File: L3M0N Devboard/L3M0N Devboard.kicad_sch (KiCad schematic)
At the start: 13 parts, among them U2 RP2040

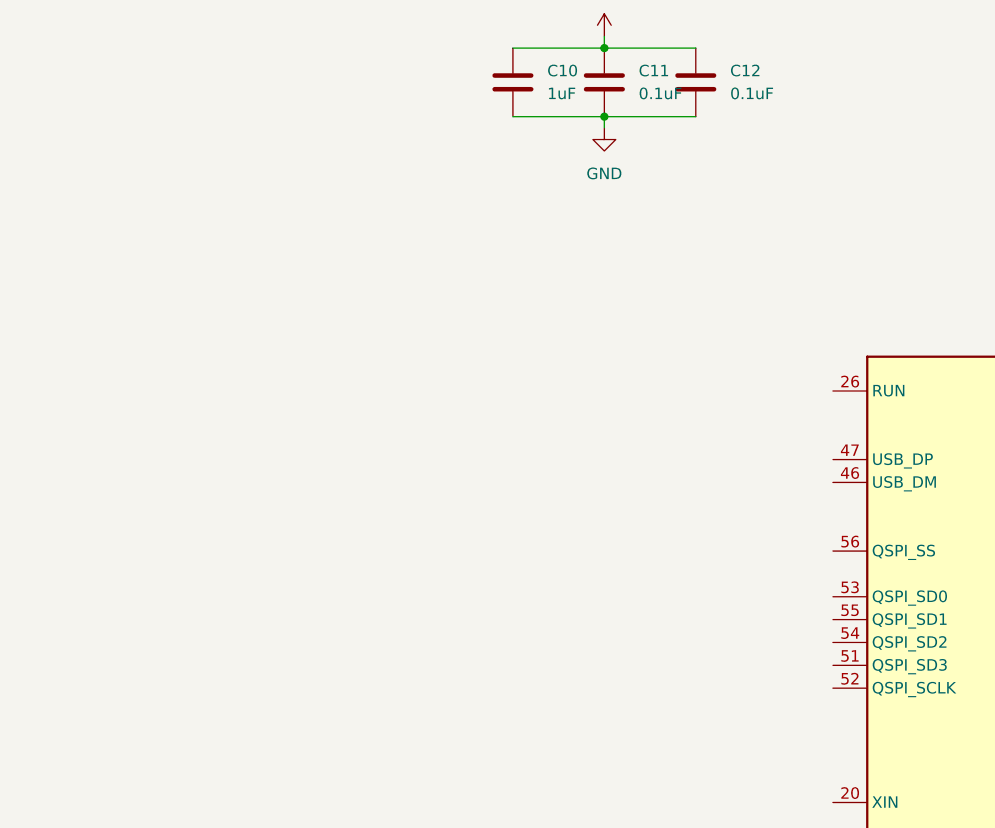
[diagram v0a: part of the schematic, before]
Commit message: Added USB C receptacle
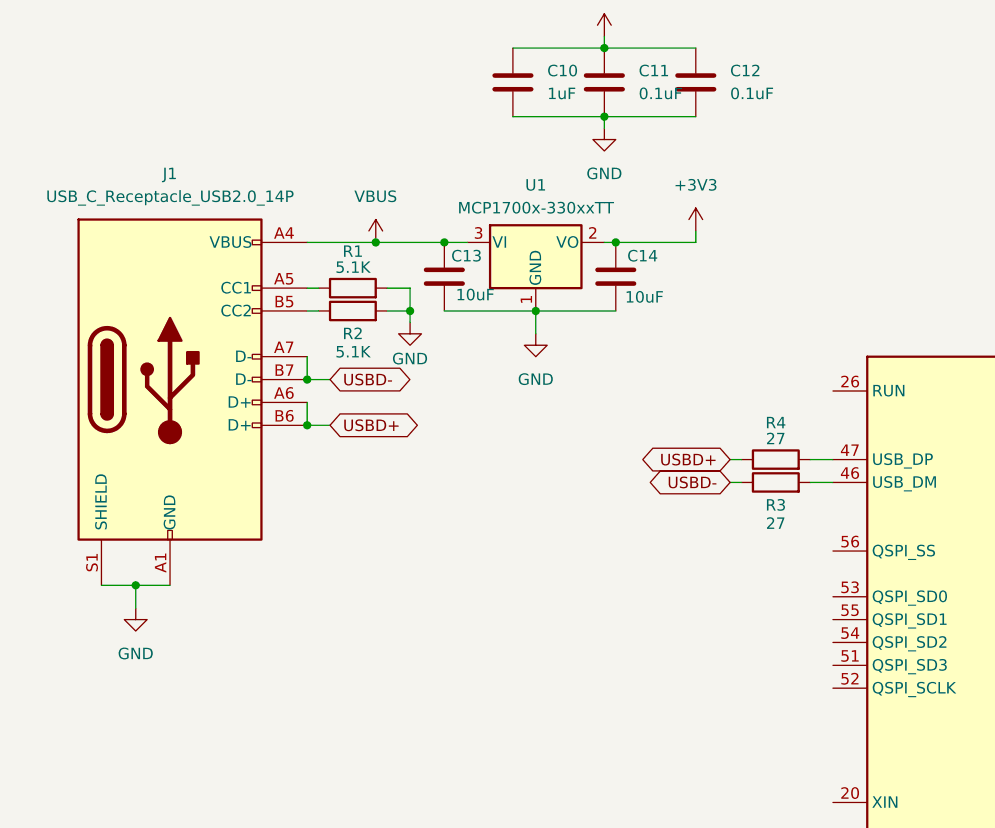
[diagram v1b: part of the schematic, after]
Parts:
- added C13, C14: 10uF, symbol Device:C
- added J1: USB_C_Receptacle_USB2.0_14P, symbol Connector:USB_C_Receptacle_USB2.0_14P
- added R1, R2: 5.1K, symbol Device:R
- added R3, R4: 27, symbol Device:R
- added U1: MCP1700x-330xxTT, Package_TO_SOT_SMD:SOT-23, symbol Regulator_Linear:MCP1700x-330xxTT
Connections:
- net +3V3: now also C14.1, U1.2 (VO)
- net GND: now also C13.2, C14.2, J1.A1 (GND), J1.A12 (GND), J1.B1 (GND), J1.B12 (GND), J1.S1 (SHIELD), R1.2, R2.2, U1.1 (GND)
- net at U2.46 (USB_DM): now also R3.2
- net at U2.47 (USB_DP): now also R4.2
- new net: J1.B5 (CC2), R2.1
- new net: J1.A5 (CC1), R1.1
- new net USBD+: J1.A6 (D+), J1.B6 (D+), R4.1
- new net USBD-: J1.A7 (D-), J1.B7 (D-), R3.1
- new net VBUS: C13.1, J1.A4 (VBUS), J1.A9 (VBUS), J1.B4 (VBUS), J1.B9 (VBUS), U1.3 (VI)

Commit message: Added crystal oscilator
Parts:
- added C15, C16: 33pF, symbol Device:C
- added R5: 1K, symbol Device:R
- added Y1: 12 MHz, symbol Device:Crystal_GND24
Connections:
- net GND: now also C15.2, C16.1, Y1.2, Y1.4
- net XIN: now reaches U2.20 (XIN)
- net XIN: now also C15.1, Y1.3
- net XOUT: now reaches U2.21 (XOUT)
- net XOUT: now also R5.2
- new net: C16.2, R5.1, Y1.1

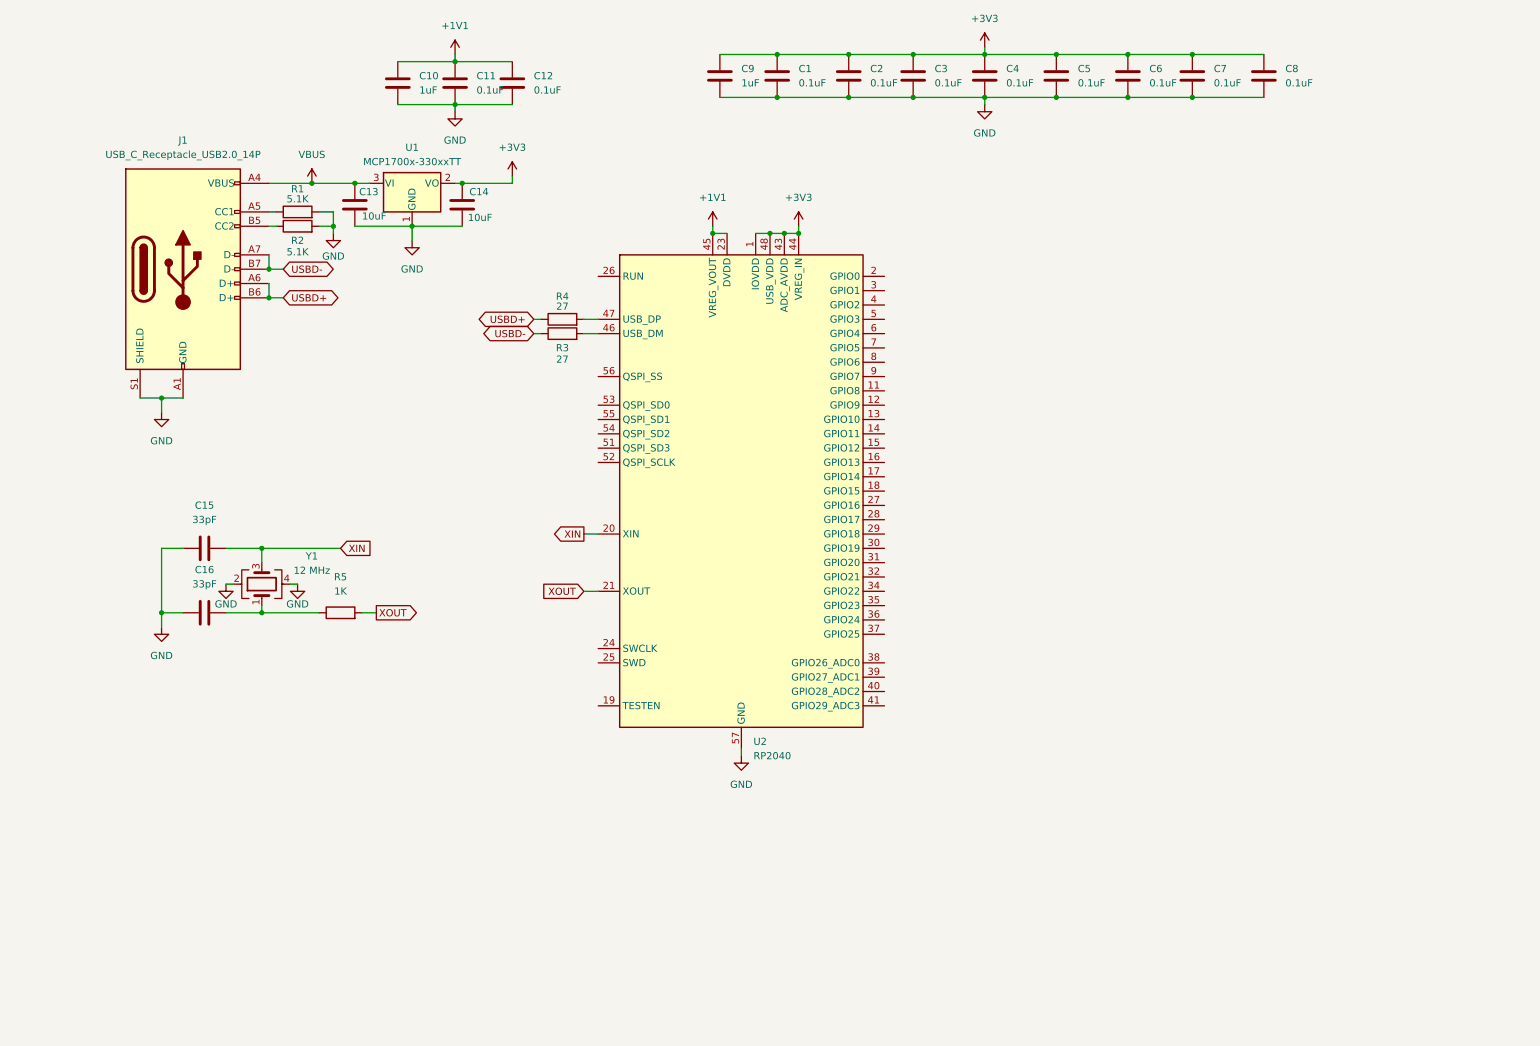
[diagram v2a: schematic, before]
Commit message: Assigned footrprints
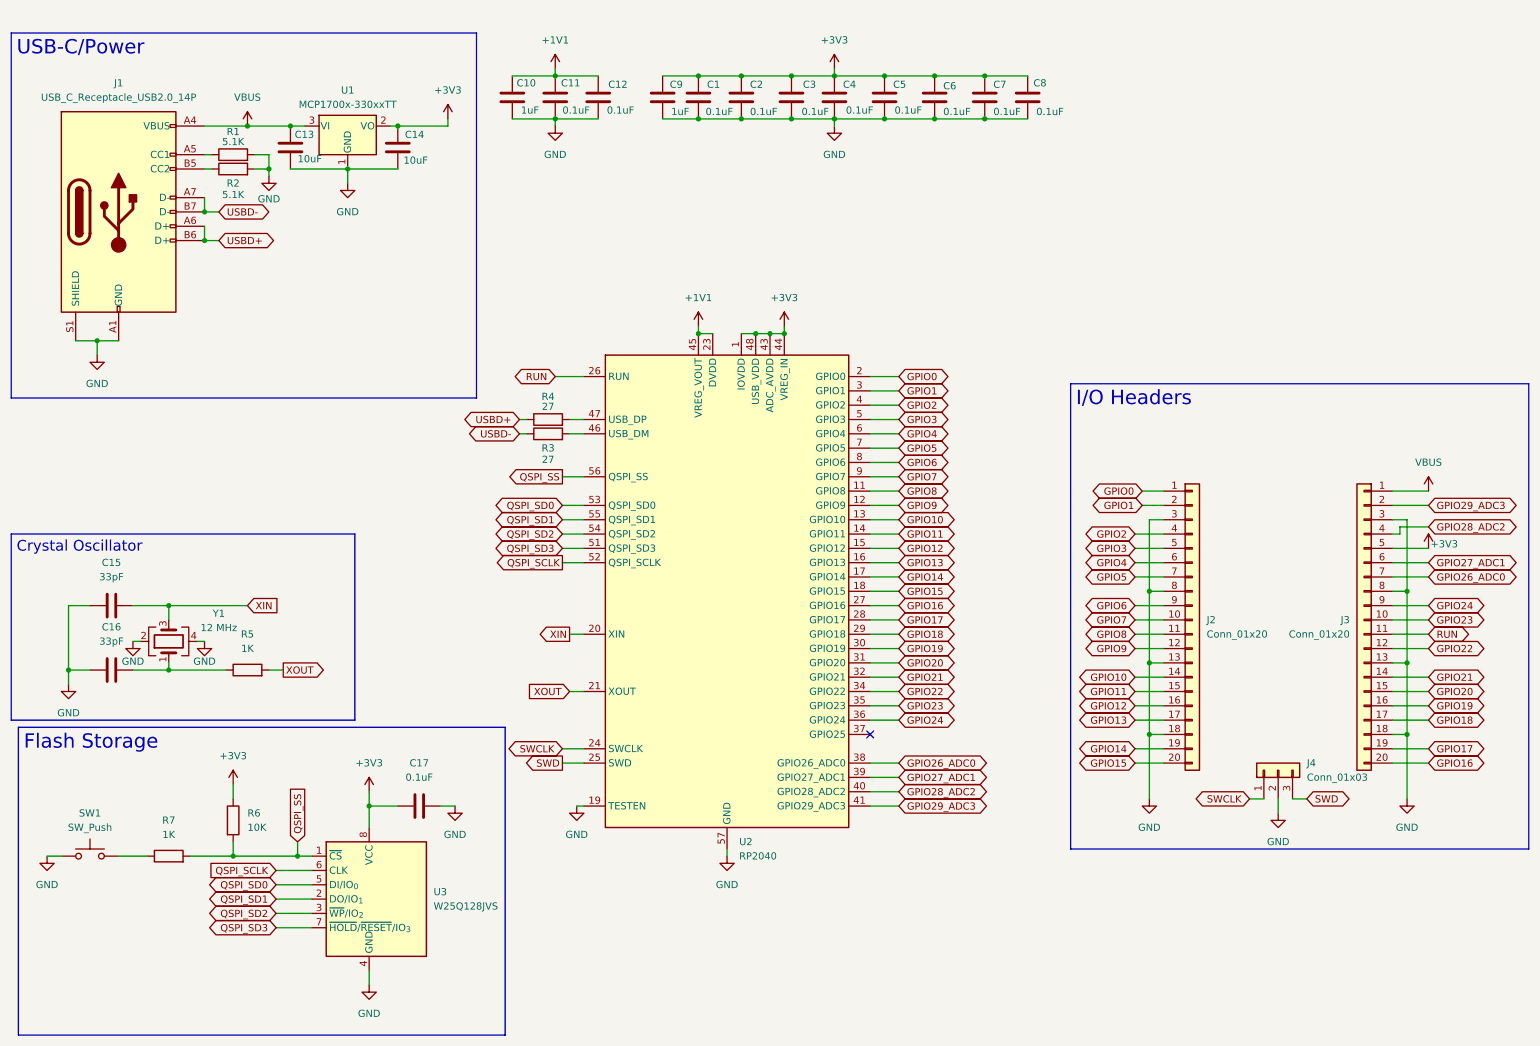
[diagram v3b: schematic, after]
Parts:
- added C17: 0.1uF, Capacitor_SMD:C_0402_1005Metric, symbol Device:C
- added J2, J3: Conn_01x20, Connector_PinHeader_2.54mm:PinHeader_1x20_P2.54mm_Vertical, symbol Connector_Generic:Conn_01x20
- added J4: Conn_01x03, Connector_PinHeader_2.54mm:PinHeader_1x03_P2.54mm_Vertical, symbol Connector_Generic:Conn_01x03
- added R6: 10K, Resistor_SMD:R_0402_1005Metric, symbol Device:R
- added R7: 1K, Resistor_SMD:R_0402_1005Metric, symbol Device:R
- added SW1: SW_Push, Button_Switch_SMD:SW_Push_SPST_NO_Alps_SKRK, symbol Switch:SW_Push
- added U3: W25Q128JVS, Package_SO:SOIC-8_5.3x5.3mm_P1.27mm, symbol Memory_Flash:W25Q128JVS
- C1, C10, C11, C12, C15, C16, C2, C3, C4, C5, C6, C7, C8, C9: footprint (none) -> Capacitor_SMD:C_0402_1005Metric
- C13, C14: footprint (none) -> Capacitor_SMD:C_0603_1608Metric
- J1: footprint (none) -> Connector_USB:USB_C_Receptacle_HRO_TYPE-C-31-M-12
- R1, R2, R3, R4, R5: footprint (none) -> Resistor_SMD:R_0402_1005Metric
- Y1: footprint (none) -> Crystal:Crystal_SMD_3225-4Pin_3.2x2.5mm
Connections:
- net +3V3: now also C17.1, J3.5 (Pin_5), R6.1, U3.8 (VCC)
- net GND: now also U2.19 (TESTEN), C17.2, J2.13 (Pin_13), J2.18 (Pin_18), J2.3 (Pin_3), J2.8 (Pin_8), J3.13 (Pin_13), J3.18 (Pin_18), J3.3 (Pin_3), J3.8 (Pin_8), J4.2 (Pin_2), SW1.1, U3.4 (GND)
- net VBUS: now also J3.1 (Pin_1)
- net GPIO8: now reaches U2.11 (GPIO8)
- net GPIO8: now also J2.11 (Pin_11)
- net GPIO9: now reaches U2.12 (GPIO9)
- net GPIO9: now also J2.12 (Pin_12)
- net GPIO10: now reaches U2.13 (GPIO10)
- net GPIO10: now also J2.14 (Pin_14)
- net GPIO11: now reaches U2.14 (GPIO11)
- net GPIO11: now also J2.15 (Pin_15)
- net GPIO12: now reaches U2.15 (GPIO12)
- net GPIO12: now also J2.16 (Pin_16)
- net GPIO13: now reaches U2.16 (GPIO13)
- net GPIO13: now also J2.17 (Pin_17)
- net GPIO14: now reaches U2.17 (GPIO14)
- net GPIO14: now also J2.19 (Pin_19)
- net GPIO15: now reaches U2.18 (GPIO15)
- net GPIO15: now also J2.20 (Pin_20)
- net GPIO0: now reaches U2.2 (GPIO0)
- net GPIO0: now also J2.1 (Pin_1)
- net SWCLK: now reaches U2.24 (SWCLK)
- net SWCLK: now also J4.1 (Pin_1)
- net SWD: now reaches U2.25 (SWD)
- net SWD: now also J4.3 (Pin_3)
- net RUN: now reaches U2.26 (RUN)
- net RUN: now also J3.11 (Pin_11)
- net GPIO16: now reaches U2.27 (GPIO16)
- net GPIO16: now also J3.20 (Pin_20)
- net GPIO17: now reaches U2.28 (GPIO17)
- net GPIO17: now also J3.19 (Pin_19)
- net GPIO18: now reaches U2.29 (GPIO18)
- net GPIO18: now also J3.17 (Pin_17)
- net GPIO1: now reaches U2.3 (GPIO1)
- net GPIO1: now also J2.2 (Pin_2)
- net GPIO19: now reaches U2.30 (GPIO19)
- net GPIO19: now also J3.16 (Pin_16)
- net GPIO20: now reaches U2.31 (GPIO20)
- net GPIO20: now also J3.15 (Pin_15)
- net GPIO21: now reaches U2.32 (GPIO21)
- net GPIO21: now also J3.14 (Pin_14)
- net GPIO22: now reaches U2.34 (GPIO22)
- net GPIO22: now also J3.12 (Pin_12)
- net GPIO23: now reaches U2.35 (GPIO23)
- net GPIO23: now also J3.10 (Pin_10)
- net GPIO24: now reaches U2.36 (GPIO24)
- net GPIO24: now also J3.9 (Pin_9)
- net GPIO26_ADC0: now reaches U2.38 (GPIO26_ADC0)
- net GPIO26_ADC0: now also J3.7 (Pin_7)
- net GPIO27_ADC1: now reaches U2.39 (GPIO27_ADC1)
- net GPIO27_ADC1: now also J3.6 (Pin_6)
- net GPIO2: now reaches U2.4 (GPIO2)
- net GPIO2: now also J2.4 (Pin_4)
- net GPIO28_ADC2: now reaches U2.40 (GPIO28_ADC2)
- net GPIO28_ADC2: now also J3.4 (Pin_4)
- net GPIO29_ADC3: now reaches U2.41 (GPIO29_ADC3)
- net GPIO29_ADC3: now also J3.2 (Pin_2)
- net GPIO3: now reaches U2.5 (GPIO3)
- net GPIO3: now also J2.5 (Pin_5)
- net QSPI_SD3: now reaches U2.51 (QSPI_SD3)
- net QSPI_SD3: now also U3.7 (~{HOLD}/~{RESET}/IO_{3})
- net QSPI_SCLK: now reaches U2.52 (QSPI_SCLK)
- net QSPI_SCLK: now also U3.6 (CLK)
- net QSPI_SD0: now reaches U2.53 (QSPI_SD0)
- net QSPI_SD0: now also U3.5 (DI/IO_{0})
- net QSPI_SD2: now reaches U2.54 (QSPI_SD2)
- net QSPI_SD2: now also U3.3 (~{WP}/IO_{2})
- net QSPI_SD1: now reaches U2.55 (QSPI_SD1)
- net QSPI_SD1: now also U3.2 (DO/IO_{1})
- net QSPI_SS: now reaches U2.56 (QSPI_SS)
- net QSPI_SS: now also R6.2, R7.2, U3.1 (~{CS})
- net GPIO4: now reaches U2.6 (GPIO4)
- net GPIO4: now also J2.6 (Pin_6)
- net GPIO5: now reaches U2.7 (GPIO5)
- net GPIO5: now also J2.7 (Pin_7)
- net GPIO6: now reaches U2.8 (GPIO6)
- net GPIO6: now also J2.9 (Pin_9)
- net GPIO7: now reaches U2.9 (GPIO7)
- net GPIO7: now also J2.10 (Pin_10)
- new net: R7.1, SW1.2
- no-connect marks 0 -> 1
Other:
- moved on the sheet: C1, C10, C11, C12, C13, C14, C15, C16, C2, C3, C4, C5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

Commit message: started some of the wiring
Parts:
- U3: value W25Q128JVS -> W25Q16JVZPIQ TR; footprint Package_SO:SOIC-8_5.3x5.3mm_P1.27mm -> Package_SON:Winbond_USON-8-1EP_3x2mm_P0.5mm_EP0.2x1.6mm
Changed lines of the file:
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@@
 			)
 		)
-		(property "Value" "W25Q128JVS"
+		(property "Value" "W25Q16JVZPIQ TR"
 			(at 87.63 172.7199 0)
 			(effects
@@
 			)
 		)
-		(property "Footprint" "Package_SO:SOIC-8_5.3x5.3mm_P1.27mm"
+		(property "Footprint" "Package_SON:Winbond_USON-8-1EP_3x2mm_P0.5mm_EP0.2x1.6mm"
 			(at 76.2 148.59 0)
 			(effects
